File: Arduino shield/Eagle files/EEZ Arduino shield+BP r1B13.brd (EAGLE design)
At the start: 175 x 105 mm, 185 parts, among them IC1 TLC5925, IC10 SN74LV125APW, IC11 SI8620EC-B-IS, IC12 SI8620EC-B-IS, IC13 Si8660EC-B-IS1, IC14 PCA21125, IC15 AT25256B, IC16 ENC28J60-I/SS, IC17 BC857BS, IC18 NE555D, IC19 BC857BS, IC2 SN74LVCC3245ADBRSSOP, IC20 NE555D, IC21 SN74LV1T34, IC3 SN74LVCC3245ADBRSSOP, IC4 SN74LVCC3245ADBRSSOP, IC5 SN74LVCC3245ADBRSSOP, IC6 LD1117ADT33TR, IC7 SN74LVCC3245ADBRSSOP, IC8 SN74LVCC3245ADBRSSOP, IC9 Si8660EC-B-IS1, J1 BS-244DSM-R, J2 BS-244DSM-B, J3 BS-244DSM-R, J4 BS-244DSM-G, J5 BS-244DSM-B, Q1 IRLML2246TRPBF, Q10 2N7002, Q11 2N7002, Q12 2N7002, Q13 2N7002, Q2 IRLML2246TRPBF, Q3 IRLML2246TRPBF, Q4 2N7002, Q5 IRLML2246TRPBF, Q6 2N7002, Q7 2N7002, Q8 2N7002, Q9 IRLML2246TRPBF, SW1 1301.9316, X1 282836-4, X10 LMJTAB881243M-L, X11 22-23-2031, X12 22-23-2031, X2 MC000005, X3 282836-4, X4 MC000005, X5 22-23-2021, X6 22-23-2041, X7 09185106324, X8 09185106324, X9 22-23-2021, Y1 32,768kHz, Y2 25MHz

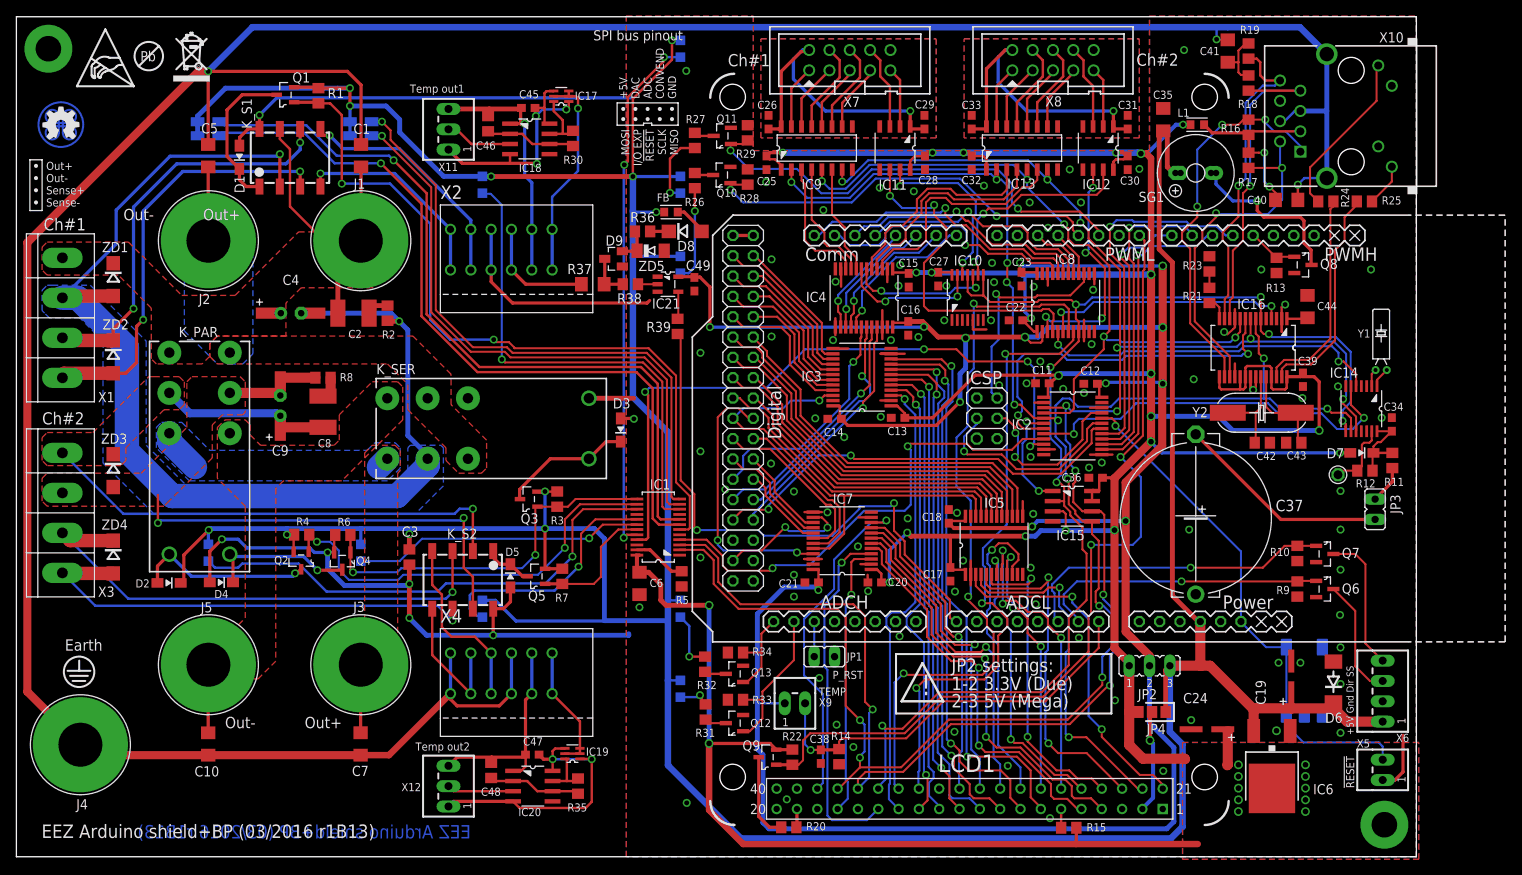
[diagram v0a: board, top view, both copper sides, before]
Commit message: Arduino Shield r1B13 BOM updated
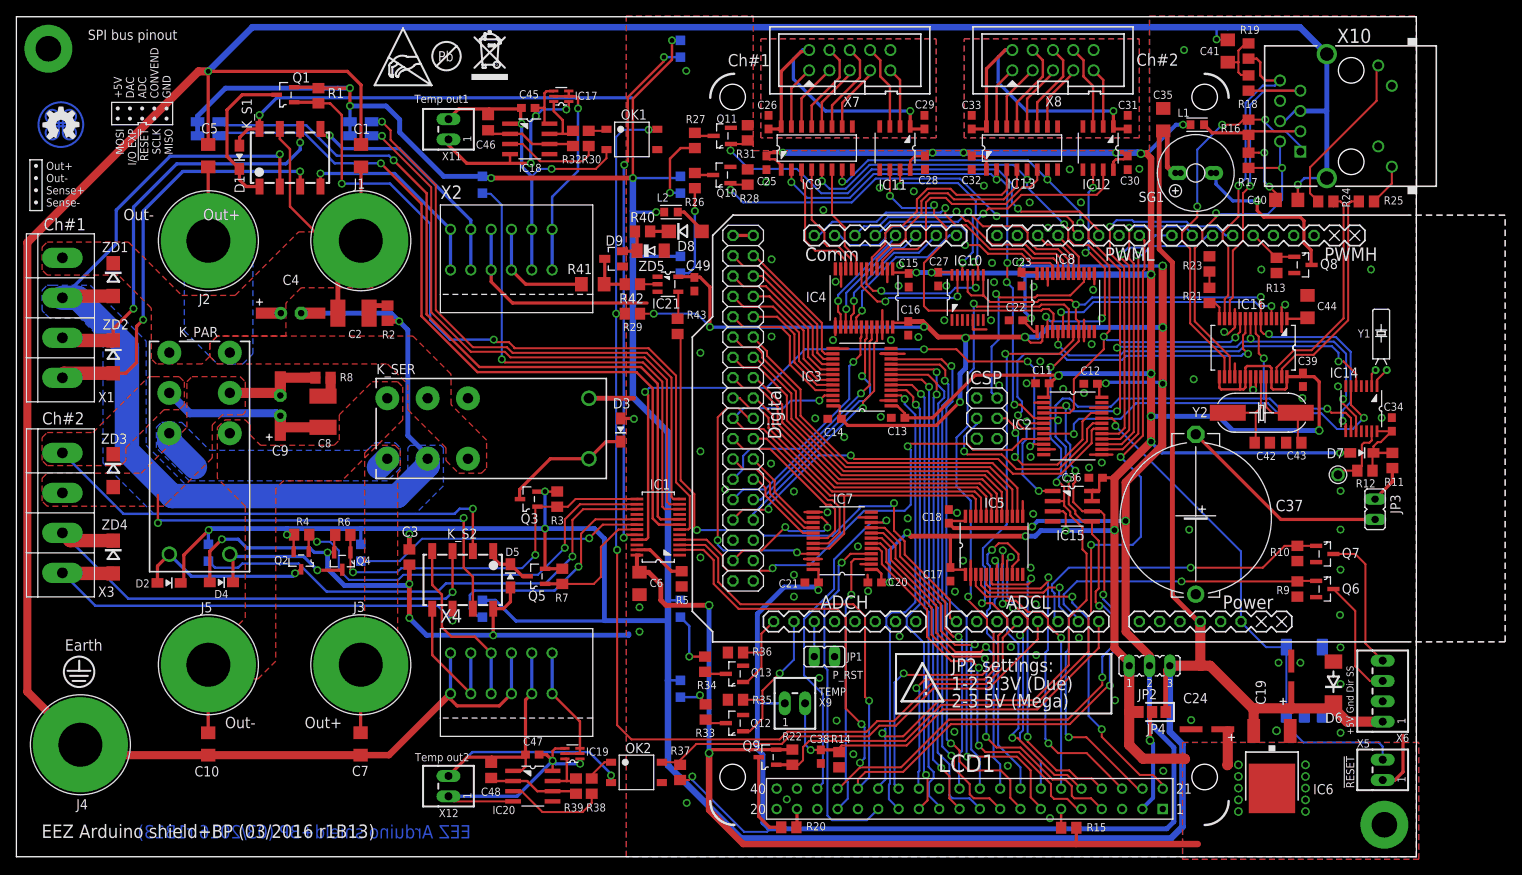
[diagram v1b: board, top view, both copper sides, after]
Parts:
- added OK1, OK2: HCPL-181, EEZ_Lib1:HCPL-181
- added R40: 100R, rcl:R0805
- added R41: 10K, resistor:R1206
- added R42, R43: 1K, rcl:R0805
- J1, J3: value BS-244DSM-R -> BS-244DSM-R
- J4: value BS-244DSM-G -> BS-244DSM-G
- J5: value BS-244DSM-B -> BS-244DSM-B
- LED_CC1, LED_CC2: value L-934ID -> HSMH-C170
- R29: value 100K -> 1K5
- R30: value 1K5 -> 180R
- R31: value 240R -> 100K
- R32: value 240R -> 1K5
- R33, R34: value 100K -> 240R
- R35: value 1K5 -> 100K
- R36: value 100R -> 100K
- R37: value 10K -> 1K5; device resistor:R1206 -> rcl:R0805
- R38: value 1K -> 180R
- R39: value 1K -> 1K5
- X10: device MyLib6:RJ45-TRAFO-LED -> EEZ_Lib1:RJ45-TRAFO-LED
- X11, X12: value 22-23-2031 -> 22-23-2021; device con-molex:22-23-2031 -> con-molex:22-23-2021
- moved R31 72.6 mm to (117.4, 90.5), turned to 90 degrees
- moved R32 67.8 mm to (95.6, 89.8), turned to 270 degrees
- moved R38 62.9 mm to (97.9, 8.83), turned to 90 degrees
- moved R37 62.0 mm to (109.0, 10.5), turned to 90 degrees
- moved R39 58.9 mm to (95.9, 8.83), turned to 270 degrees
- moved R36 53.9 mm to (115.9, 25.5), turned to 180 degrees
- moved U$2 37.3 mm to (82.9, 97.1)
- moved U$4 37.2 mm to (70.8, 96.4)
- moved U$3 37.2 mm to (79.8, 100.1)
- moved R29 26.8 mm to (103.0, 67.9), turned to 180 degrees
- moved R35 22.5 mm to (115.9, 19.6), turned to 180 degrees
- moved R34 4.08 mm to (112.1, 24.1), turned to 90 degrees
- moved R33 4.04 mm to (112.1, 18.1), turned to 270 degrees
- moved R30 1.97 mm to (97.5, 89.8), turned to 90 degrees
- moved R14 0.38 mm to (128.8, 12.1)
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- renumbered FB to L2, LED1 to LED_01_POS, LED2 to LED_01_NEG
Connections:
- removed net WATCHDOG: MCU.A5
- new net BATT_NTC1: MCU.A4, OK1.4, R29.2
- new net BATT_NTC2: MCU.A3, OK2.4, R37.2
- new net N$22: OK1.1, R30.2
- new net N$36: OK2.1, R38.2
- net EXT_TRIG: now also R43.1; no longer R39.1
- net GND: now also OK1.3, OK2.3, R31.2, R35.2, R36.2; no longer R29.2, R33.2, R34.2
- net GND_CH1: now also OK1.2, X11.2; no longer X11.3
- net GND_CH2: now also OK2.2, X12.2; no longer X12.3
- net LED_CC2: now also R35.1; no longer R33.1
- net LED_CV1: now also R31.1; no longer R29.1
- net LED_CV2: now also R36.1; no longer R34.1
- net N$1: now also R43.2; no longer R39.2
- net N$12: now also R33.2; no longer R31.2
- net N$14: now also R34.2; no longer R32.2
- net N$15: now also R33.1; no longer R31.1
- net N$16: now also R32.2; no longer R30.2
- net N$17: now also R39.1; no longer R35.1
- net N$18: now also R32.1; no longer R30.1
- net N$19: now also R39.2; no longer R35.2
- net N$2: now also R40.1; no longer R36.1
- net N$23: now also R34.1; no longer R32.1
- net N$26: now also R41.2, R42.2; no longer R37.2, R38.2
- net N$27: now also R42.1; no longer R38.1
- net N$33: now also R40.2; no longer R36.2
- net N$4: now also R41.1; no longer R37.1
- net TEMP_FREQ1: now also R30.1; no longer X11.2
- net TEMP_FREQ2: now also R38.1; no longer X12.2
- net VCC: now also R29.1, R37.1
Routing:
- net BATT_NTC1: track 0.00 -> 139.4 mm, vias 0 -> 3
- net BATT_NTC2: track 0.00 -> 56.2 mm
- net GND_CH2: track 27.4 -> 51.7 mm, vias 0 -> 1
- net VCC: track 329.6 -> 353.7 mm, vias 13 -> 15
- net GND_CH1: track 32.6 -> 44.2 mm, vias 1 -> 2
- net TEMP_FREQ2: track 8.34 -> 12.6 mm
- net TEMP_FREQ1: track 8.52 -> 12.2 mm
- net N$36: track 0.00 -> 3.52 mm
- net +5V_CH2: track 36.8 -> 33.6 mm
- net N$22: track 0.00 -> 2.30 mm
- net ETH_LEDA: track 26.8 -> 28.4 mm
- net 3V3LCD_DB6: track 33.5 -> 34.6 mm
- net 3V3MISO: track 156.7 -> 157.3 mm
- net GND: track 240.4 -> 239.9 mm, vias 98 -> 101
- net LED_CC2: track 19.2 -> 19.3 mm, vias 0 -> 1
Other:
- board text added: "OK1"
- board text added: "OK2"
- board text added: "R40"
- board text added: "R41"
- board text added: "R42"
- board text added: "R43"
- board text removed: "LED1"
- board text removed: "LED2"
- board text removed: "LED_CC1"
- board text removed: "LED_CC2"
- board text removed: "LED_CV1"
- board text removed: "LED_CV2"
- board text removed: "LED_O2+"
- board text removed: "LED_O2-"
- board text removed: "LED_PWR"
- board text removed: "LED_S1"
- board text removed: "LED_S2"
- board text removed: "SW1"
